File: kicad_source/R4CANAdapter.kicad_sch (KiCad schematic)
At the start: 29 parts, among them CN1 CONN_01X05, CN2 691322310004, CN3 GH_SM04B-GHS-TB, CN4 GH_SM04B-GHS-TB, CN5 SM04B-SRSS-TB, Q1 2N7002, Q2 2N7002, U1 TCAN332GDR, U2 24LC64

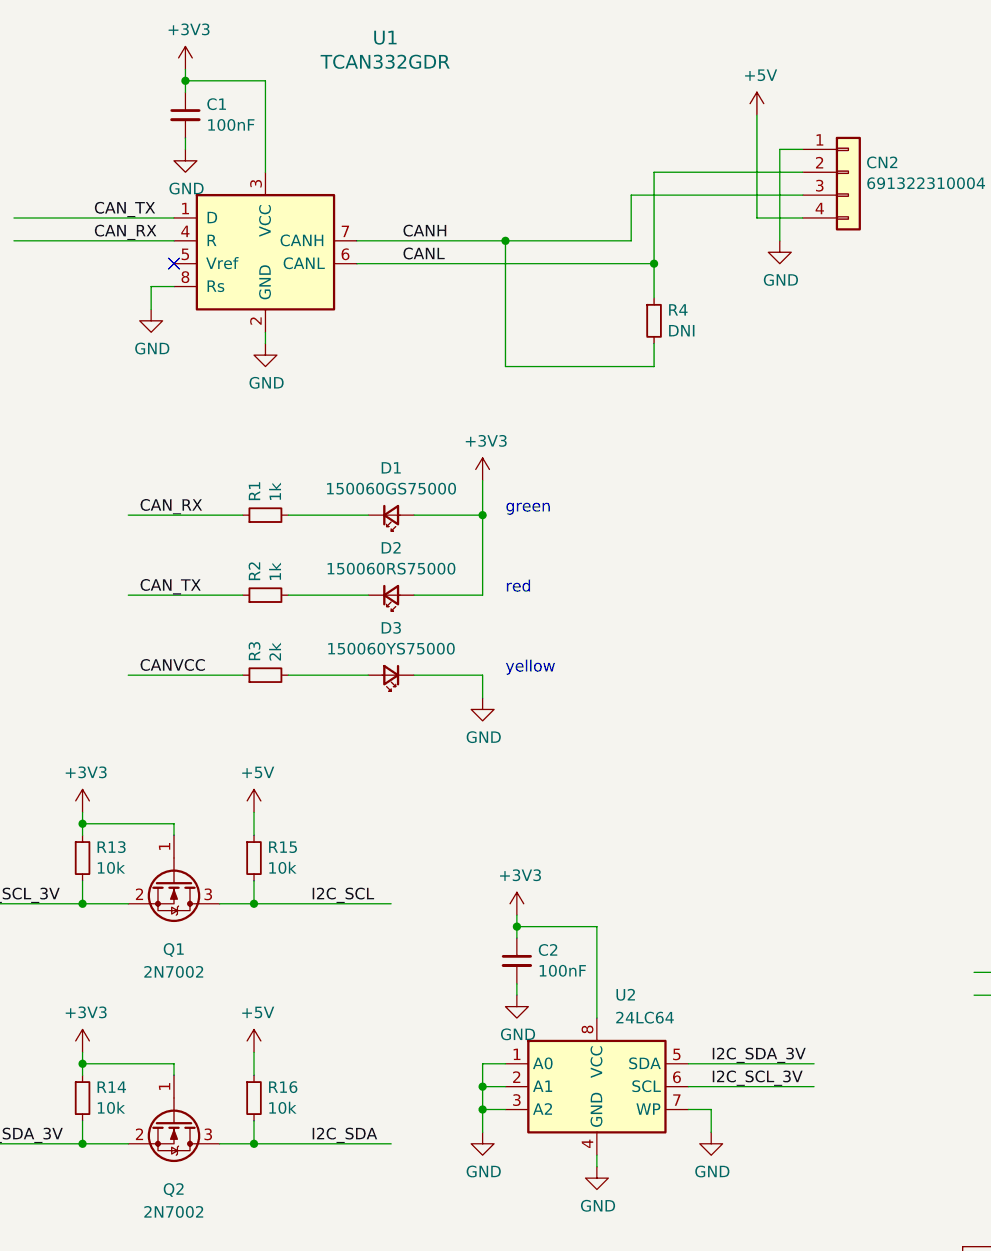
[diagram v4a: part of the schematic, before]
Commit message: switched I2C eeprom and CAN driver to the 5V domain
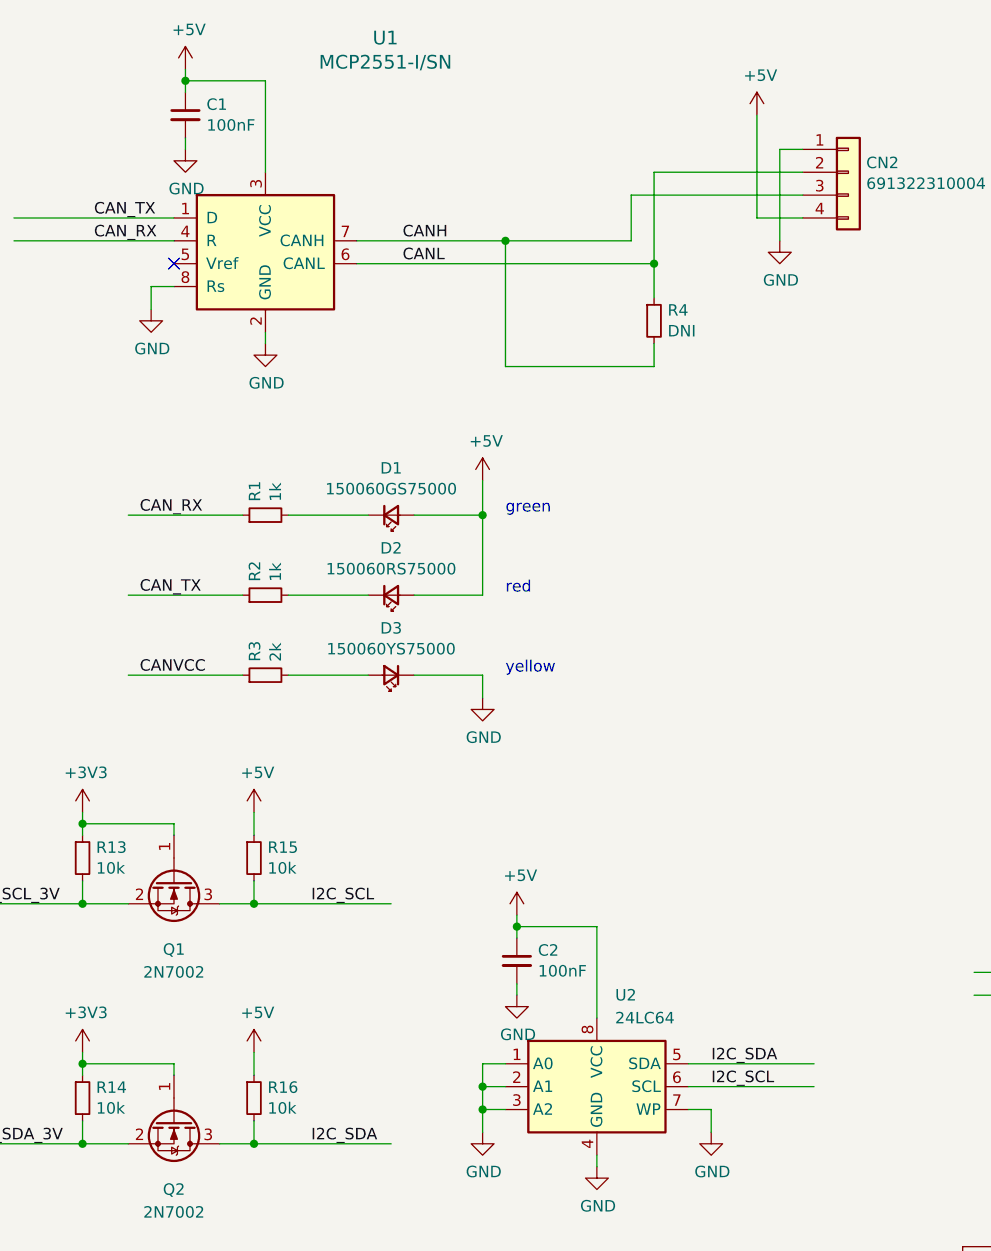
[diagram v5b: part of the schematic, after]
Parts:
- U1: value TCAN332GDR -> MCP2551-I/SN
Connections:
- net +3V3: no longer C1.1, C2.1, D1.2 (A), D2.2 (A), U1.3 (VCC), U2.8 (VCC)
- net +5V: now also C1.1, C2.1, D1.2 (A), D2.2 (A), U1.3 (VCC), U2.8 (VCC)
- net I2C_SCL: now also U2.6 (SCL)
- net I2C_SCL_3V: no longer U2.6 (SCL)
- net I2C_SDA: now also U2.5 (SDA)
- net I2C_SDA_3V: no longer U2.5 (SDA)
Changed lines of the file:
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@@
     (effects (font (size 1.27 1.27)) (justify left bottom))
   )
-  (label "I2C_SDA_3V" (at 194.31 132.08 0)
+  (label "I2C_SDA" (at 194.31 132.08 0)
     (effects (font (size 1.27 1.27)) (justify left bottom))
   )
@@
     (effects (font (size 1.27 1.27)) (justify left bottom))
   )
-  (label "I2C_SCL_3V" (at 194.31 134.62 0)
+  (label "I2C_SCL" (at 194.31 134.62 0)
     (effects (font (size 1.27 1.27)) (justify left bottom))
   )
@@
       (effects (font (size 1.524 1.524)))
     )
-    (property "Value" "TCAN332GDR" (id 1) (at 158.115 20.8026 0)
+    (property "Value" "MCP2551-I/SN" (id 1) (at 158.115 20.8026 0)
       (effects (font (size 1.524 1.524)))
     )
@@
     (pin "1")
     (pin "2")
-  )
-  (symbol (lib_id "power:+3V3") (at 135.89 21.59 0) (unit 1)
-    (in_bom yes) (on_board yes)
-    (property "Reference" "#PWR04" (id 0) (at 135.89 25.4 0)
-      (effects (font (size 1.27 1.27)) hide)
-    )
-    (property "Value" "+3V3" (id 1) (at 136.271 17.1958 0))
-    (property "Footprint" "" (id 2) (at 135.89 21.59 0))
-    (property "Datasheet" "" (id 3) (at 135.89 21.59 0))
-    (pin "1")
   )
   (symbol (lib_id "power:GND") (at 135.89 30.48 0) (unit 1)
@@
     (pin "1")
   )
-  (symbol (lib_id "power:+3V3") (at 168.91 67.31 0) (unit 1)
-    (in_bom yes) (on_board yes)
-    (property "Reference" "#PWR0101" (id 0) (at 168.91 71.12 0)
-      (effects (font (size 1.27 1.27)) hide)
-    )
-    (property "Value" "+3V3" (id 1) (at 169.291 62.9158 0))
-    (property "Footprint" "" (id 2) (at 168.91 67.31 0))
-    (property "Datasheet" "" (id 3) (at 168.91 67.31 0))
-    (pin "1")
-  )
   (symbol (lib_id "power:GND") (at 144.78 52.07 0) (unit 1)
     (in_bom yes) (on_board yes)
@@
     (pin "3")
   )
-  (symbol (lib_id "power:+3V3") (at 172.72 115.57 0) (unit 1)
-    (in_bom yes) (on_board yes)
-    (property "Reference" "#PWR017" (id 0) (at 172.72 119.38 0)
-      (effects (font (size 1.27 1.27)) hide)
-    )
-    (property "Value" "+3V3" (id 1) (at 173.101 111.1758 0))
-    (property "Footprint" "" (id 2) (at 172.72 115.57 0))
-    (property "Datasheet" "" (id 3) (at 172.72 115.57 0))
-    (pin "1")
-  )
   (symbol (lib_id "Device:R_Small") (at 124.46 135.89 0) (unit 1)
     (in_bom yes) (on_board yes)
@@
     (pin "1")
     (pin "2")
+  )
+  (symbol (lib_id "power:+5V") (at 168.91 67.31 0) (unit 1)
+    (in_bom yes) (on_board yes)
+    (property "Reference" "#PWR?" (id 0) (at 168.91 71.12 0)
+      (effects (font (size 1.27 1.27)) hide)
+    )
+    (property "Value" "+5V" (id 1) (at 169.291 62.9158 0))
+    (property "Footprint" "" (id 2) (at 168.91 67.31 0))
+    (property "Datasheet" "" (id 3) (at 168.91 67.31 0))
+    (pin "1")
   )
   (symbol (lib_id "power:GND") (at 172.72 124.46 0) (unit 1)
@@
     (property "Footprint" "" (id 2) (at 172.72 124.46 0))
     (property "Datasheet" "" (id 3) (at 172.72 124.46 0))
+    (pin "1")
+  )
+  (symbol (lib_id "power:+5V") (at 172.72 115.57 0) (unit 1)
+    (in_bom yes) (on_board yes)
+    (property "Reference" "#PWR?" (id 0) (at 172.72 119.38 0)
+      (effects (font (size 1.27 1.27)) hide)
+    )
+    (property "Value" "+5V" (id 1) (at 173.101 111.1758 0))
+    (property "Footprint" "" (id 2) (at 172.72 115.57 0))
+    (property "Datasheet" "" (id 3) (at 172.72 115.57 0))
     (pin "1")
   )
@@
     (pin "1")
   )
+  (symbol (lib_id "power:+5V") (at 135.89 21.59 0) (unit 1)
+    (in_bom yes) (on_board yes)
+    (property "Reference" "#PWR?" (id 0) (at 135.89 25.4 0)
+      (effects (font (size 1.27 1.27)) hide)
+    )
+    (property "Value" "+5V" (id 1) (at 136.271 17.1958 0))
+    (property "Footprint" "" (id 2) (at 135.89 21.59 0))
+    (property "Datasheet" "" (id 3) (at 135.89 21.59 0))
+    (pin "1")
+  )
   (symbol (lib_id "Jumper:Jumper_3_Bridged12") (at 44.45 143.51 0) (unit 1)
     (in_bom yes) (on_board yes) (fields_autoplaced)
@@
       (reference "#PWR03") (unit 1) (value "+3V3") (footprint "")
     )
-    (path "/00000000-0000-0000-0000-00005fd75219"
-      (reference "#PWR04") (unit 1) (value "+3V3") (footprint "")
-    )
     (path "/00000000-0000-0000-0000-00005fd7521f"
       (reference "#PWR05") (unit 1) (value "GND") (footprint "")
@@
       (reference "#PWR016") (unit 1) (value "GND") (footprint "")
     )
-    (path "/5c33e2a2-68e2-42af-b6fb-e267d7979d85"
-      (reference "#PWR017") (unit 1) (value "+3V3") (footprint "")
-    )
     (path "/6dc16533-1083-44c6-a105-efff521c3a3c"
       (reference "#PWR018") (unit 1) (value "GND") (footprint "")
@@
       (reference "#PWR022") (unit 1) (value "GND") (footprint "")
     )
-    (path "/00000000-0000-0000-0000-0000600f7b1b"
-      (reference "#PWR0101") (unit 1) (value "+3V3") (footprint "")
-    )
     (path "/063533ff-8f07-472b-a1e2-8256bc1bd8ef"
       (reference "#PWR0102") (unit 1) (value "GND") (footprint "")
@@
       (reference "#PWR0103") (unit 1) (value "GND") (footprint "")
     )
+    (path "/6d9c3a0b-7adb-47b1-8a99-67115e282304"
+      (reference "#PWR?") (unit 1) (value "+5V") (footprint "")
+    )
+    (path "/7a0ec2e4-ddc8-4899-ae39-365cbb651538"
+      (reference "#PWR?") (unit 1) (value "+5V") (footprint "")
+    )
+    (path "/87dbd9e6-ae8c-4bf0-855c-399d6eecdf9f"
+      (reference "#PWR?") (unit 1) (value "+5V") (footprint "")
+    )
     (path "/00000000-0000-0000-0000-00005fd75213"
       (reference "C1") (unit 1) (value "100nF") (footprint "Capacitor_SMD:C_0603_1608Metric")
@@
     )
     (path "/00000000-0000-0000-0000-00005fd751ff"
-      (reference "U1") (unit 1) (value "TCAN332GDR") (footprint "Package_SO:SO-8_3.9x4.9mm_P1.27mm")
+      (reference "U1") (unit 1) (value "MCP2551-I/SN") (footprint "Package_SO:SO-8_3.9x4.9mm_P1.27mm")
     )
     (path "/22be3d4d-ae12-4eb8-846f-0339b769d4f7"

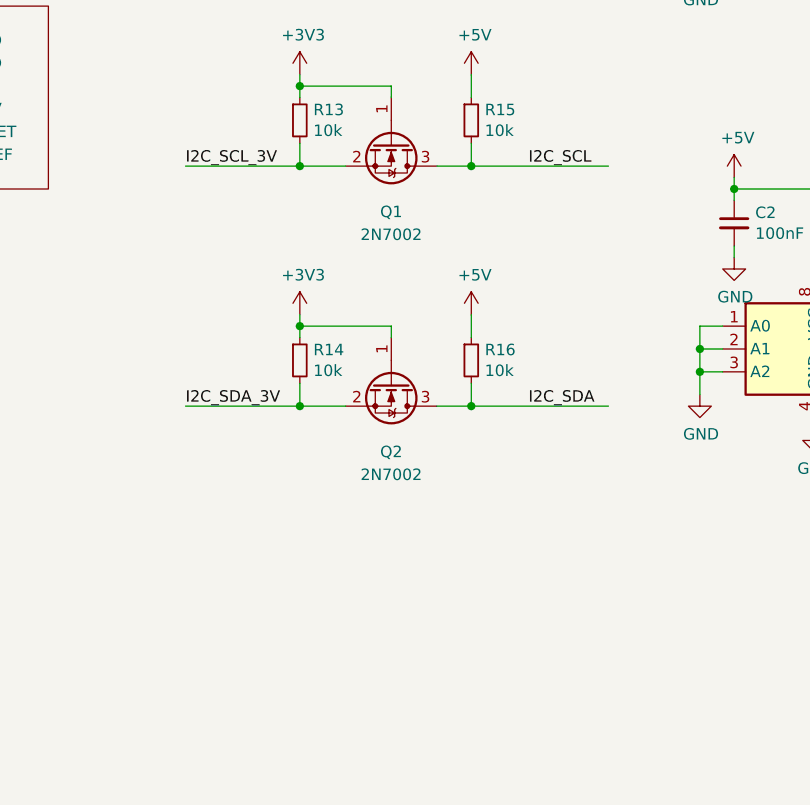
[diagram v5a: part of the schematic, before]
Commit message: added bypass resistors for I2C circuit
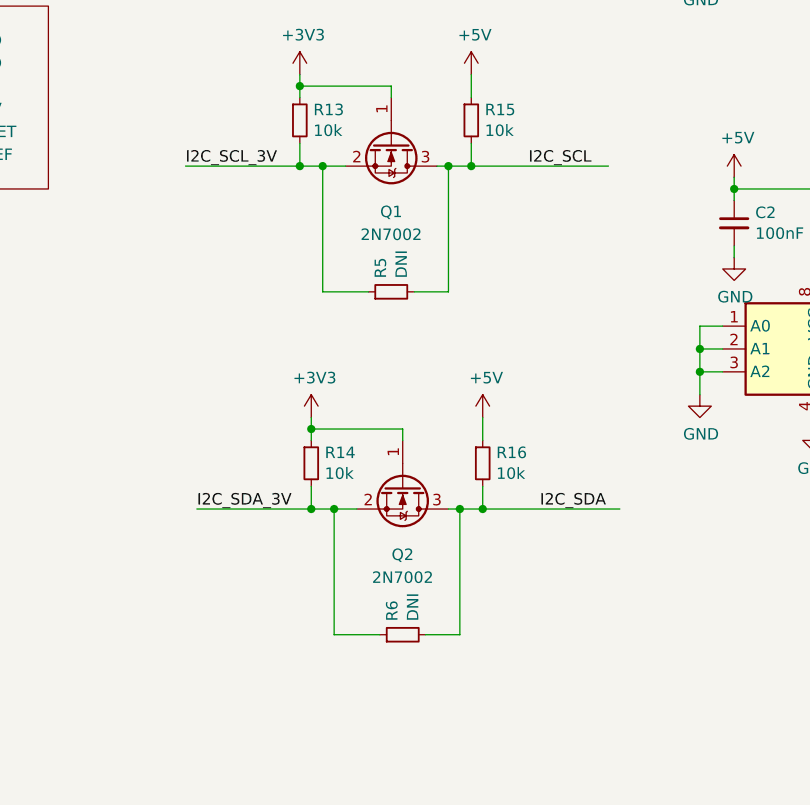
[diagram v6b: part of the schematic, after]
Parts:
- added R5, R6: DNI, Resistor_SMD:R_0603_1608Metric, symbol Device:R_Small
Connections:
- net I2C_SCL: now also R5.2
- net I2C_SCL_3V: now also R5.1
- net I2C_SDA: now also R6.2
- net I2C_SDA_3V: now also R6.1
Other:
- moved on the sheet: Q2, R14, R16

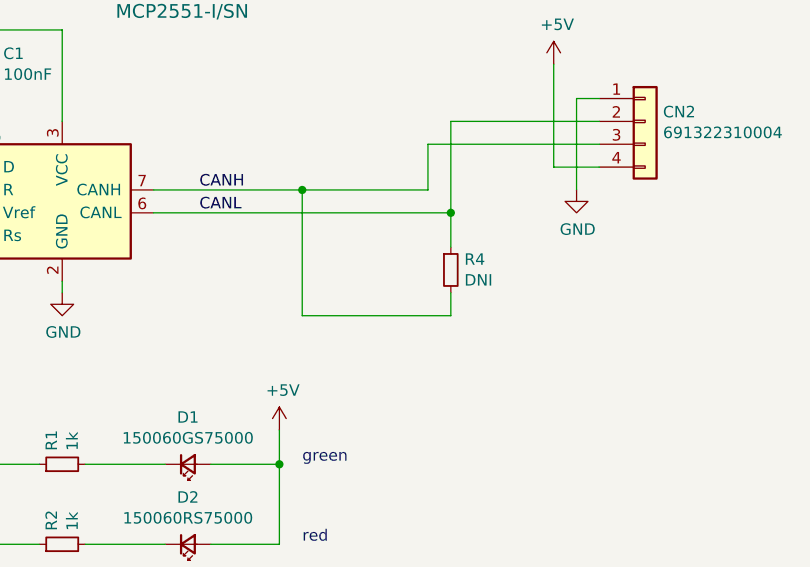
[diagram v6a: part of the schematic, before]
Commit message: added jumper for CAN termination
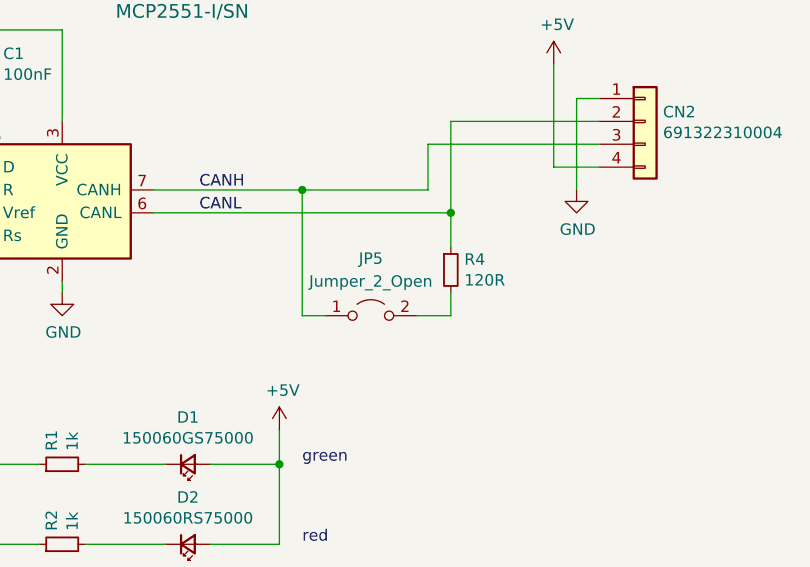
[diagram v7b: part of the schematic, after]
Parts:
- added JP5: Jumper_2_Open, Connector_PinHeader_2.54mm:PinHeader_1x02_P2.54mm_Vertical, symbol Jumper:Jumper_2_Open
- R4: value DNI -> 120R
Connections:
- net CANH: now also JP5.1 (A); no longer R4.2
- new net: JP5.2 (B), R4.2
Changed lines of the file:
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@@
   (title_block
     (title "R4CANAdapter")
-    (date "2023-08-16")
+    (date "2023-08-18")
     (rev "0.1")
     (company "generationmake")
@@
     (stroke (width 0) (type default) (color 0 0 0 0))
   )
-  (wire (pts (xy 187.96 54.61) (xy 171.45 54.61))
-    (stroke (width 0) (type default) (color 0 0 0 0))
-  )
   (wire (pts (xy 168.91 132.08) (xy 168.91 134.62))
     (stroke (width 0) (type default) (color 0 0 0 0))
@@
     (stroke (width 0) (type default) (color 0 0 0 0))
   )
+  (wire (pts (xy 171.45 54.61) (xy 173.99 54.61))
+    (stroke (width 0) (type default) (color 0 0 0 0))
+  )
   (wire (pts (xy 133.35 166.37) (xy 128.27 166.37))
     (stroke (width 0) (type default) (color 0 0 0 0))
@@
     (stroke (width 0) (type default) (color 0 0 0 0))
   )
+  (wire (pts (xy 184.15 54.61) (xy 187.96 54.61))
+    (stroke (width 0) (type default) (color 0 0 0 0))
+  )
   (wire (pts (xy 181.61 116.84) (xy 181.61 127))
     (stroke (width 0) (type default) (color 0 0 0 0))
@@
       (effects (font (size 1.27 1.27)) (justify left))
     )
-    (property "Value" "DNI" (id 1) (at 189.4586 50.673 0)
+    (property "Value" "120R" (id 1) (at 189.4586 50.673 0)
       (effects (font (size 1.27 1.27)) (justify left))
     )
@@
     (pin "1")
   )
+  (symbol (lib_id "Jumper:Jumper_2_Open") (at 179.07 54.61 0) (unit 1)
+    (in_bom yes) (on_board yes) (fields_autoplaced)
+    (property "Reference" "JP5" (id 0) (at 179.07 48.26 0))
+    (property "Value" "Jumper_2_Open" (id 1) (at 179.07 50.8 0))
+    (property "Footprint" "Connector_PinHeader_2.54mm:PinHeader_1x02_P2.54mm_Vertical" (id 2) (at 179.07 54.61 0)
+      (effects (font (size 1.27 1.27)) hide)
+    )
+    (property "Datasheet" "~" (id 3) (at 179.07 54.61 0)
+      (effects (font (size 1.27 1.27)) hide)
+    )
+    (pin "1")
+    (pin "2")
+  )
   (symbol (lib_id "power:+3V3") (at 124.46 104.14 0) (unit 1)
     (in_bom yes) (on_board yes)
@@
       (reference "JP4") (unit 1) (value "Jumper_3_Bridged12") (footprint "Connector_PinHeader_2.54mm:PinHeader_1x03_P2.54mm_Vertical")
     )
+    (path "/326aaf4a-f3e8-40d8-bc72-4a00b2755d2e"
+      (reference "JP5") (unit 1) (value "Jumper_2_Open") (footprint "Connector_PinHeader_2.54mm:PinHeader_1x02_P2.54mm_Vertical")
+    )
     (path "/00000000-0000-0000-0000-00005fd7a91a"
       (reference "L1") (unit 1) (value "Label") (footprint "generationmake:generationmake_small_silk")
@@
     )
     (path "/00000000-0000-0000-0000-00005fd751ac"
-      (reference "R4") (unit 1) (value "DNI") (footprint "Resistor_SMD:R_0603_1608Metric")
+      (reference "R4") (unit 1) (value "120R") (footprint "Resistor_SMD:R_0603_1608Metric")
     )
     (path "/0b73b1f9-a76d-46b9-8e78-0d0ed0a2d813"
